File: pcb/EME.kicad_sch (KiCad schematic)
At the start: 68 parts, among them J1 BMP180, J10 Reset, J11 UART2, J12 SPI_CONN, J13 UART0, J14 MQ135, J16 OUT, J17 OE, J18 GPIO's, J19 I2C, J2 ReedSwitchX8, J20 Jumper, J3 SS41, J4 Hoja Mojada, J5 PanelSolar, J6 BH1750, J7 DHT22, J8 Baterias, J9 Jumper, Q1 IRF540N, Q2 IRF540N, SW1 Enable, U1 LM78M05_TO220, U3 74HC251, U5 TL082

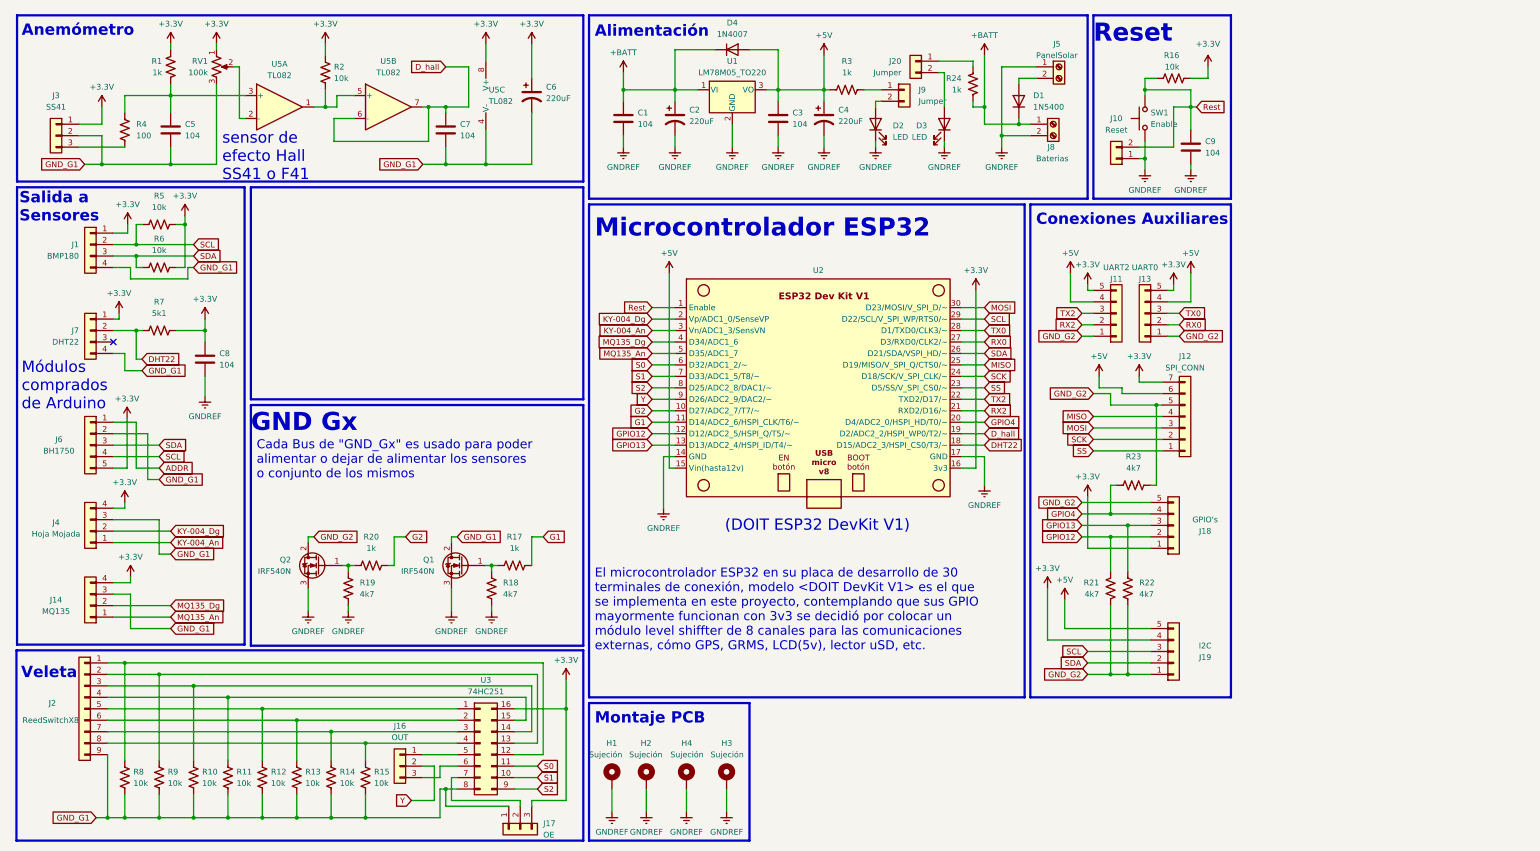
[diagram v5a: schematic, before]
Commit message: Nueva versión de la PCB, se saca a parte veleta y anemómetro en placas aparte con los sensores
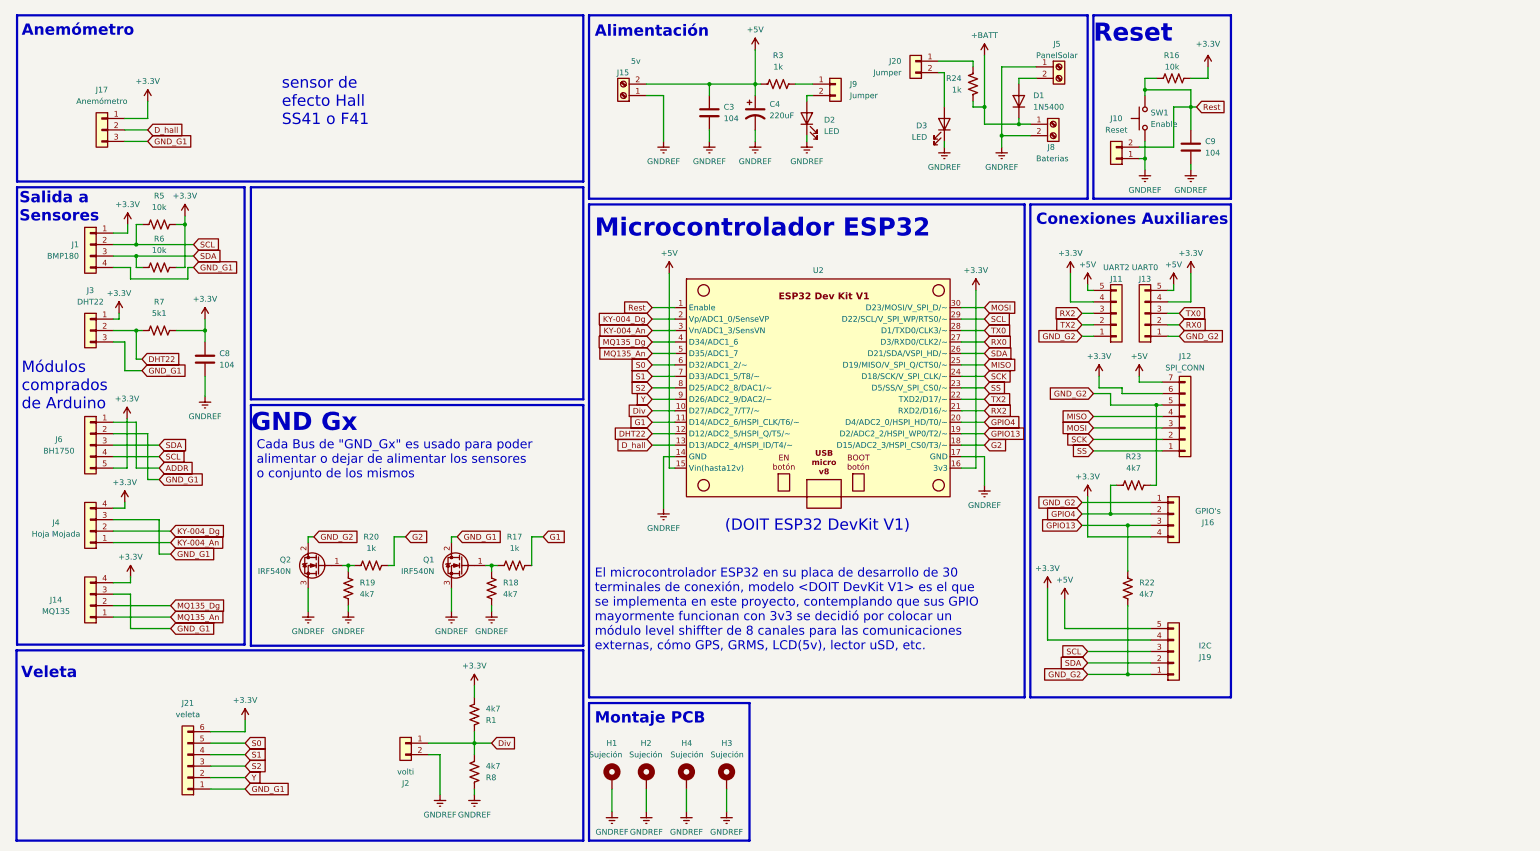
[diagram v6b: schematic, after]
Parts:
- removed C1, C5, C7: 104, Capacitor_THT:C_Disc_D4.3mm_W1.9mm_P5.00mm, symbol Device:C
- removed C2, C6: 220uF, Capacitor_THT:C_Radial_D8.0mm_H11.5mm_P3.50mm, symbol Device:C_Polarized_US
- removed D4: 1N4007, Diode_THT:D_DO-41_SOD81_P10.16mm_Horizontal, symbol Diode:1N4007
- removed J16: OUT, Connector_PinHeader_2.54mm:PinHeader_1x03_P2.54mm_Vertical, symbol Connector_Generic:Conn_01x03
- removed J18: GPIO's, Connector_PinHeader_2.54mm:PinHeader_1x05_P2.54mm_Vertical, symbol Connector_Generic:Conn_01x05
- removed J2: ReedSwitchX8, Connector_PinHeader_2.54mm:PinHeader_1x09_P2.54mm_Vertical, symbol Connector_Generic:Conn_01x09
- removed J7: DHT22, Connector_PinHeader_2.54mm:PinHeader_1x04_P2.54mm_Vertical, symbol Connector_Generic:Conn_01x04
- removed R10, R11, R12, R13, R14, R15, R2, R9: 10k, Resistor_THT:R_Axial_DIN0207_L6.3mm_D2.5mm_P10.16mm_Horizontal, symbol Device:R_US
- removed R21: 4k7, Resistor_THT:R_Axial_DIN0207_L6.3mm_D2.5mm_P10.16mm_Horizontal, symbol Device:R_US
- removed R4: 100, Resistor_THT:R_Axial_DIN0207_L6.3mm_D2.5mm_P10.16mm_Horizontal, symbol Device:R_US
- removed RV1: 100k, Potentiometer_THT:Potentiometer_Bourns_3266W_Vertical, symbol Device:R_Potentiometer_US
- removed U1: LM78M05_TO220, Package_TO_SOT_THT:TO-220-3_Vertical, symbol Regulator_Linear:LM78M05_TO220
- removed U3: 74HC251, Package_DIP:DIP-16_W7.62mm_LongPads, symbol Connector_Generic:Conn_02x08_Counter_Clockwise
- removed U5: TL082, Package_DIP:DIP-8_W7.62mm_LongPads, symbol Amplifier_Operational:TL082
- added J15: 5v, TerminalBlock_Phoenix:TerminalBlock_Phoenix_PT-1,5-2-5.0-H_1x02_P5.00mm_Horizontal, symbol Connector:Screw_Terminal_01x02
- added J16: GPIO's, Connector_PinHeader_2.54mm:PinHeader_1x04_P2.54mm_Vertical, symbol Connector_Generic:Conn_01x04
- added J2: volti, Connector_PinHeader_2.54mm:PinHeader_1x02_P2.54mm_Vertical, symbol Connector_Generic:Conn_01x02
- added J21: veleta, Connector_PinHeader_2.54mm:PinHeader_1x06_P2.54mm_Vertical, symbol Connector_Generic:Conn_01x06
- J17: value OE -> Anemómetro
- J3: value SS41 -> DHT22
- R1: value 1k -> 4k7
- R8: value 10k -> 4k7
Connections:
- net GPIO12 is gone; now on net DHT22: U2.12 (D12/ADC2_5/HSPI_Q/T5/~)
- net +3.3V: now also J11.4 (Pin_4), J12.6 (Pin_6), J13.4 (Pin_4), J17.1 (Pin_1), J16.4 (Pin_4), J21.6 (Pin_6); no longer J11.5 (Pin_5), J12.7 (Pin_7), J13.5 (Pin_5), J17.3 (Pin_3)
- net +5V: now also J11.5 (Pin_5), J12.7 (Pin_7), J13.5 (Pin_5), J15.2 (Pin_2); no longer J11.4 (Pin_4), J12.6 (Pin_6), J13.4 (Pin_4)
- net DHT22: now also J3.2 (Pin_2); no longer U2.18 (D15/ADC2_3/HSPI_CS0/T3/~)
- net D_hall: now also J17.2 (Pin_2), U2.13 (D13/ADC2_4/HSPI_ID/T4/~); no longer U2.19 (D2/ADC2_2/HSPI_WP0/T2/~)
- net G2: now also U2.18 (D15/ADC2_3/HSPI_CS0/T3/~); no longer U2.10 (D27/ADC2_7/T7/~)
- net GNDREF: now also R8.2, J15.1 (Pin_1), J2.2 (Pin_2)
- net GND_G1: now also J17.3 (Pin_3), J3.3 (Pin_3), J21.1 (Pin_1); no longer J17.1 (Pin_1), J3.2 (Pin_2), R8.2
- net GND_G2: now also J16.1 (Pin_1)
- net GPIO13: now also U2.19 (D2/ADC2_2/HSPI_WP0/T2/~), J16.3 (Pin_3); no longer U2.13 (D13/ADC2_4/HSPI_ID/T4/~)
- net GPIO4: now also J16.2 (Pin_2)
- net RX2: now also J11.3 (Pin_3); no longer J11.2 (Pin_2)
- net S0: now also J21.5 (Pin_5)
- net S1: now also J21.4 (Pin_4)
- net S2: now also J21.3 (Pin_3)
- net TX2: now also J11.2 (Pin_2); no longer J11.3 (Pin_3)
- net Y: now also J21.2 (Pin_2)
- net Div: now reaches R1.2
- net Div: now also R8.1, U2.10 (D27/ADC2_7/T7/~), J2.1 (Pin_1)
- no-connect marks 1 -> 0
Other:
- moved on the sheet: C3, C4, D2, J9, R3
